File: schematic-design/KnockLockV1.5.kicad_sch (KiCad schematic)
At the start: 44 parts, among them IC1 ESP32-C3-WROOM-02-N4, IC2 LM2575-3.3WT, IC3 MC74HC74ADTR2G, J1 2477, J2 UJ2-B-HR-G-TH, J3 TBP04R12-500-03BE, J4 UART, Q1 IRLML6402TRPBF, Q2 BC547B, Q3 BC547B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

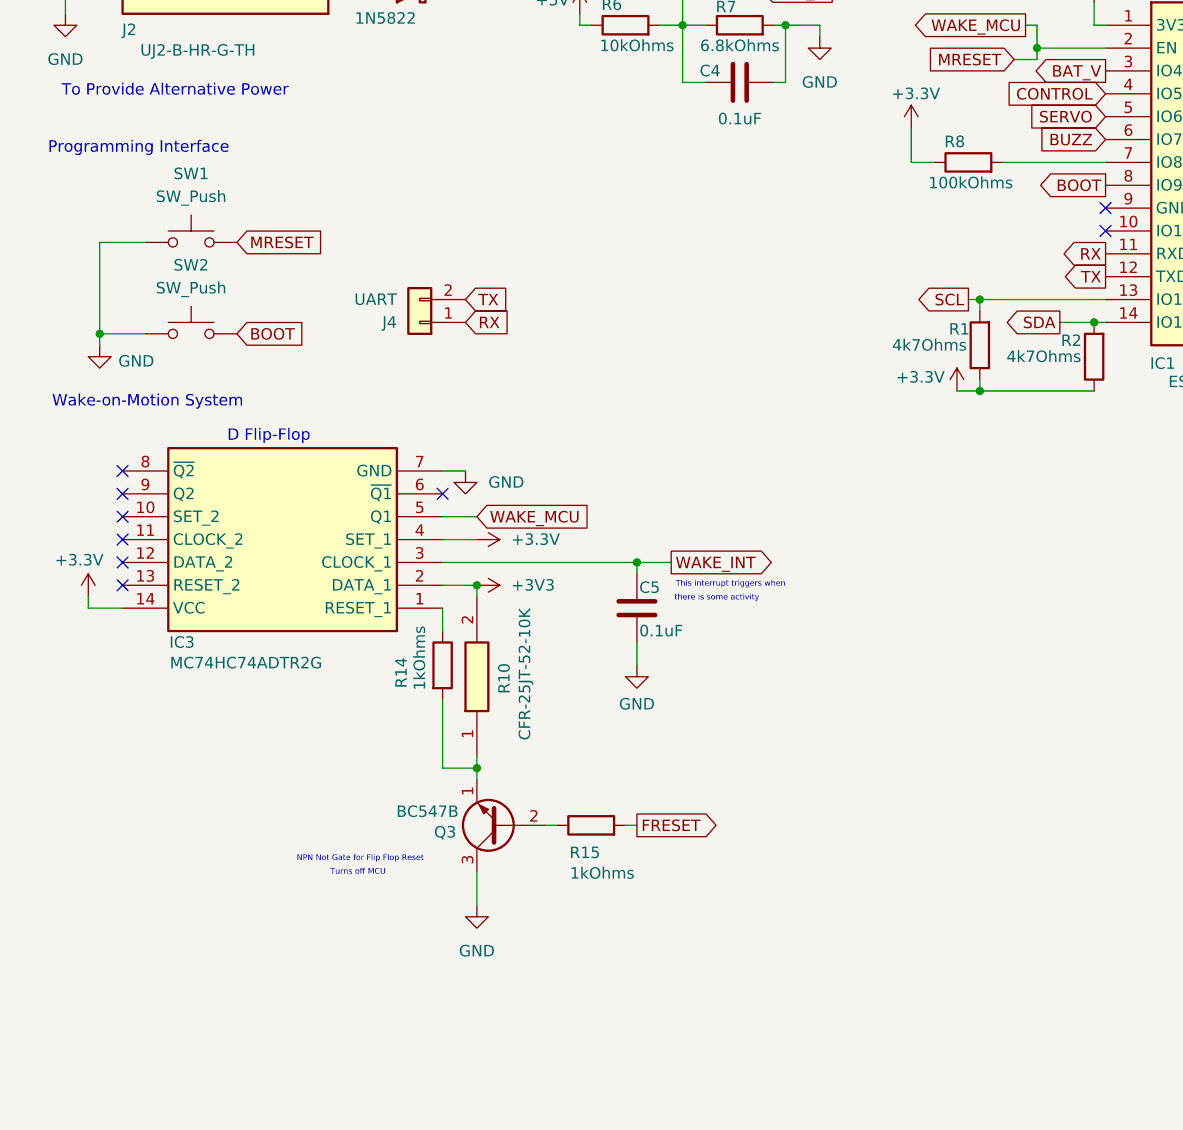
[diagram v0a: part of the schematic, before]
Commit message: Minor Update to V1.5
- added RC delay for reset button
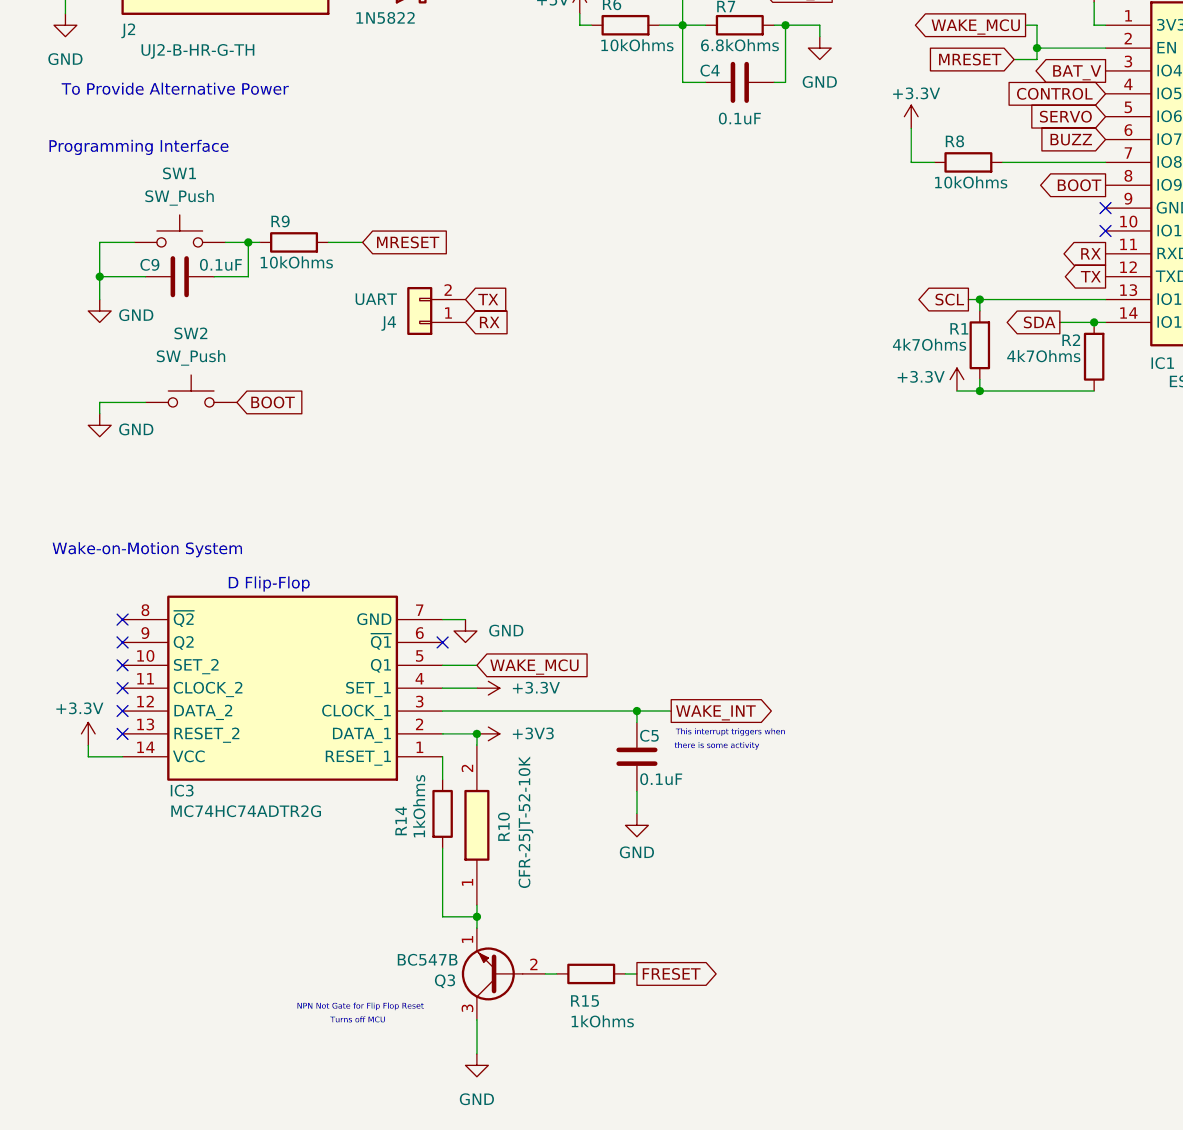
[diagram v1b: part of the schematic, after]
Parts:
- added C9: 0.1uF, symbol Device:C
- added R9: 10kOhms, SamacSys_Parts:RESAD1590W60L630D240, symbol Device:R
- R8: value 100kOhms -> 10kOhms
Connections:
- net GND: now also C9.1
- net MRESET: now also R9.2; no longer SW1.2
- new net: C9.2, R9.1, SW1.2
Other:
- moved on the sheet: C5, IC3, Q3, R10, R14, R15, SW1, SW2
